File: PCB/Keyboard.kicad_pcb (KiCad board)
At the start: 2 copper layers, 28 x 18 mm, 25 parts, among them P1 USB_OTG, SW1 RST, U1 ATMEGA32U4-QFN44, X1 ABM10-16.000MHZ-D30-T3

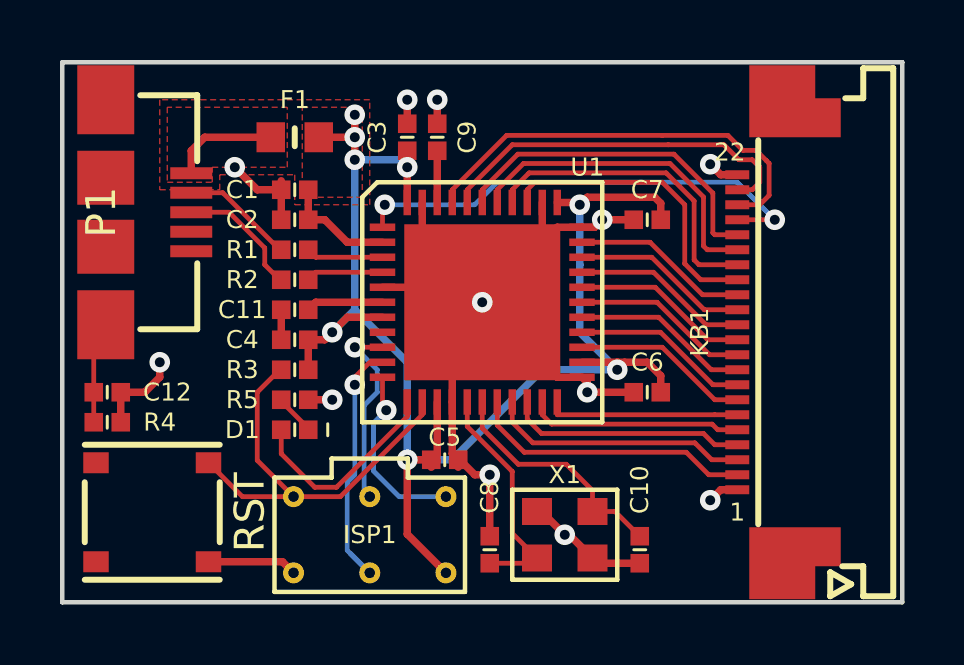
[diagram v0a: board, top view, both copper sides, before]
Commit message: Added bootloader and script for flashing
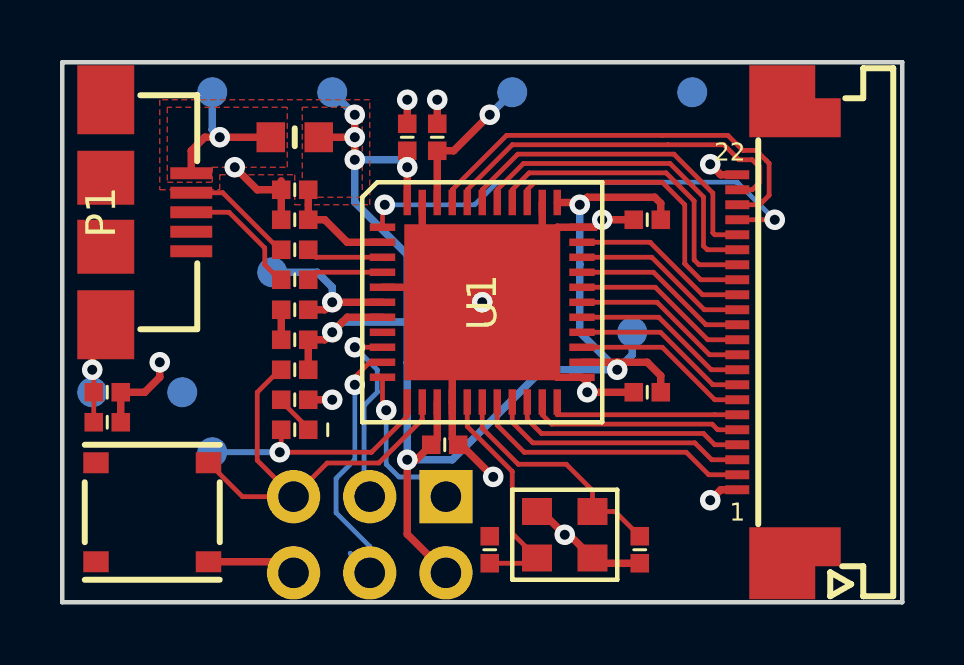
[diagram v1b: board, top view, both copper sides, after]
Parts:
- added TP1: TESTPOINT, Vias_and_Pads:TestPoint_1.0mm, B.Cu at (150.0, 109.0)
- added TP11: TESTPOINT, Vias_and_Pads:TestPoint_1.0mm, B.Cu at (154.0, 111.0)
- added TP13: TESTPOINT, Vias_and_Pads:TestPoint_1.0mm, B.Cu at (153.0, 109.0)
- added TP14: TESTPOINT, Vias_and_Pads:TestPoint_1.0mm, B.Cu at (170.0, 99.0)
- added TP2: TESTPOINT, Vias_and_Pads:TestPoint_1.0mm, B.Cu at (154.0, 99.0)
- added TP3: TESTPOINT, Vias_and_Pads:TestPoint_1.0mm, B.Cu at (158.0, 99.0)
- added TP4: TESTPOINT, Vias_and_Pads:TestPoint_1.0mm, B.Cu at (168.0, 107.0)
- added TP5: TESTPOINT, Vias_and_Pads:TestPoint_1.0mm, B.Cu at (164.0, 99.0)
- added TP6: TESTPOINT, Vias_and_Pads:TestPoint_1.0mm, B.Cu at (156.0, 105.0)
- C10, C8: value 15p -> 8p
- ISP1: footprint SMD-Connectors:ISP-PADS_2mm54 -> Pin_Header_2.54mm:PIN_HEADER-2x3
- X1: value ABM10-16.000MHZ-D30-T3 -> ECS-160-10-36Q-ES-TR
- moved C5 0.50 mm to (161.8, 110.8)
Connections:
- P1 pad 4: (no net) -> Net-(P1-Pad4)
- U1 pad 8: (no net) -> /TMP
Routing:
- net +5V: track 55.2 -> 58.7 mm
- net /VARef: track 1.72 -> 5.03 mm, vias 0 -> 1
- net /VUCap: track 2.58 -> 5.29 mm, vias 0 -> 1
- net GND: track 53.1 -> 50.7 mm
- net GNDPWR: track 3.42 -> 5.85 mm, vias 0 -> 1
- net VBUS: track 3.59 -> 5.19 mm, vias 0 -> 1
- net /LED: track 7.35 -> 8.67 mm, vias 0 -> 1
- net /MISO: track 6.12 -> 5.39 mm
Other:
- board text added: "USB Keyboard v1.2 RasmusB 2017 Psion series 5mx"
- board text removed: "USB Keyboard v1.1 RasmusB 2017 Psion Series 5/5mx"

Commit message: Restore production files
I discovered that I had overwritten the PCB files by accident. These are restored from an older version.
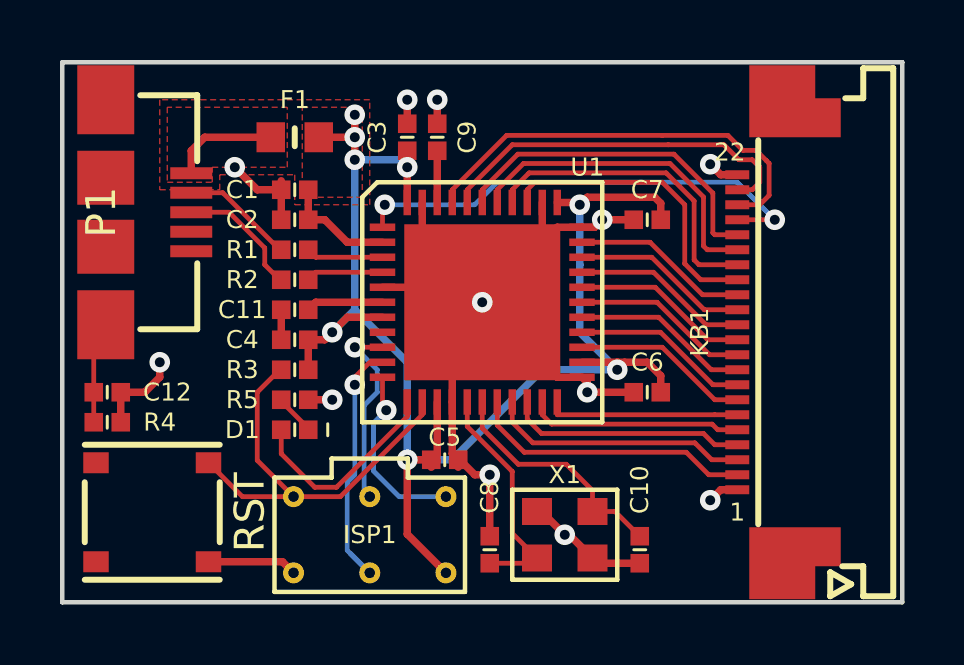
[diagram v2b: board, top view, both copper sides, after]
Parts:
- removed TP1, TP11, TP13, TP14, TP2, TP3, TP4, TP5, TP6: TESTPOINT, Vias_and_Pads:TestPoint_1.0mm
- C10, C8: value 8p -> 15p
- ISP1: footprint Pin_Header_2.54mm:PIN_HEADER-2x3 -> SMD-Connectors:ISP-PADS_2mm54
- X1: value ECS-160-10-36Q-ES-TR -> ABM10-16.000MHZ-D30-T3
- moved C5 0.50 mm to (161.8, 111.2)
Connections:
- P1 pad 4: Net-(P1-Pad4) -> (no net)
- U1 pad 8: /TMP -> (no net)
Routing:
- net +5V: track 58.7 -> 55.2 mm
- net /VARef: track 5.03 -> 1.72 mm, vias 1 -> 0
- net /VUCap: track 5.29 -> 2.58 mm, vias 1 -> 0
- net GND: track 50.7 -> 53.1 mm
- net GNDPWR: track 5.85 -> 3.42 mm, vias 1 -> 0
- net VBUS: track 5.19 -> 3.59 mm, vias 1 -> 0
- net /LED: track 8.67 -> 7.35 mm, vias 1 -> 0
- net /MISO: track 5.39 -> 6.12 mm
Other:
- board text added: "USB Keyboard v1.1 RasmusB 2017 Psion Series 5/5mx"
- board text removed: "USB Keyboard v1.2 RasmusB 2017 Psion series 5mx"
